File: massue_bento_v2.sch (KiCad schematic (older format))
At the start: 0 parts

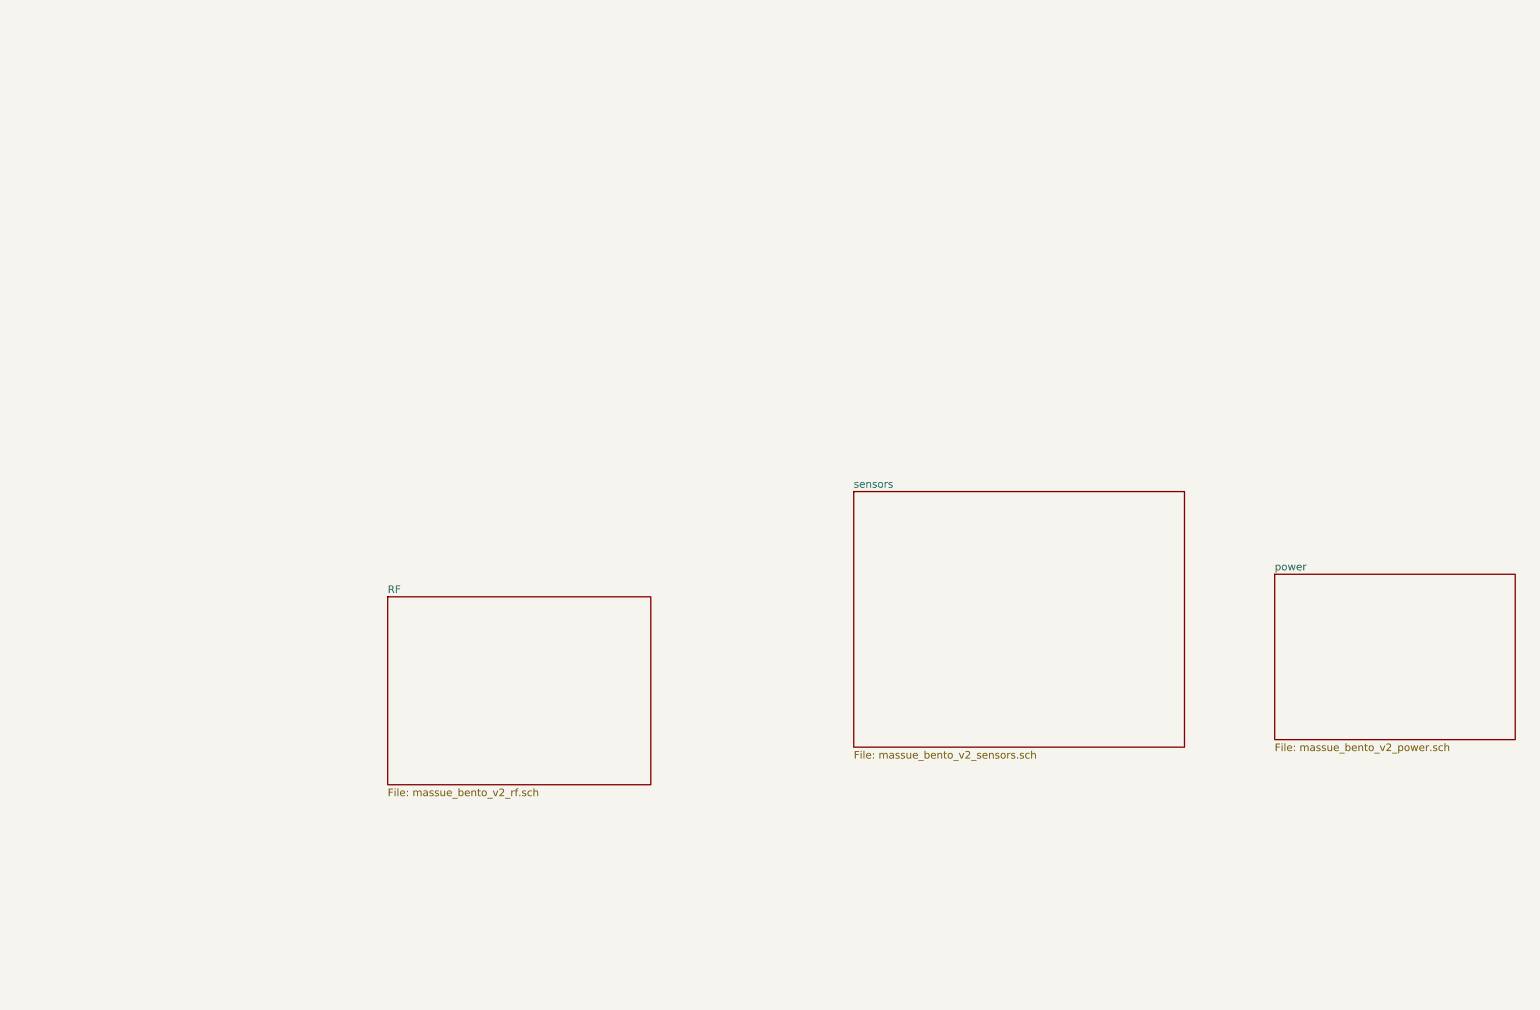
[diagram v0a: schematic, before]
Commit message: New: main MCU connections and Flash memory
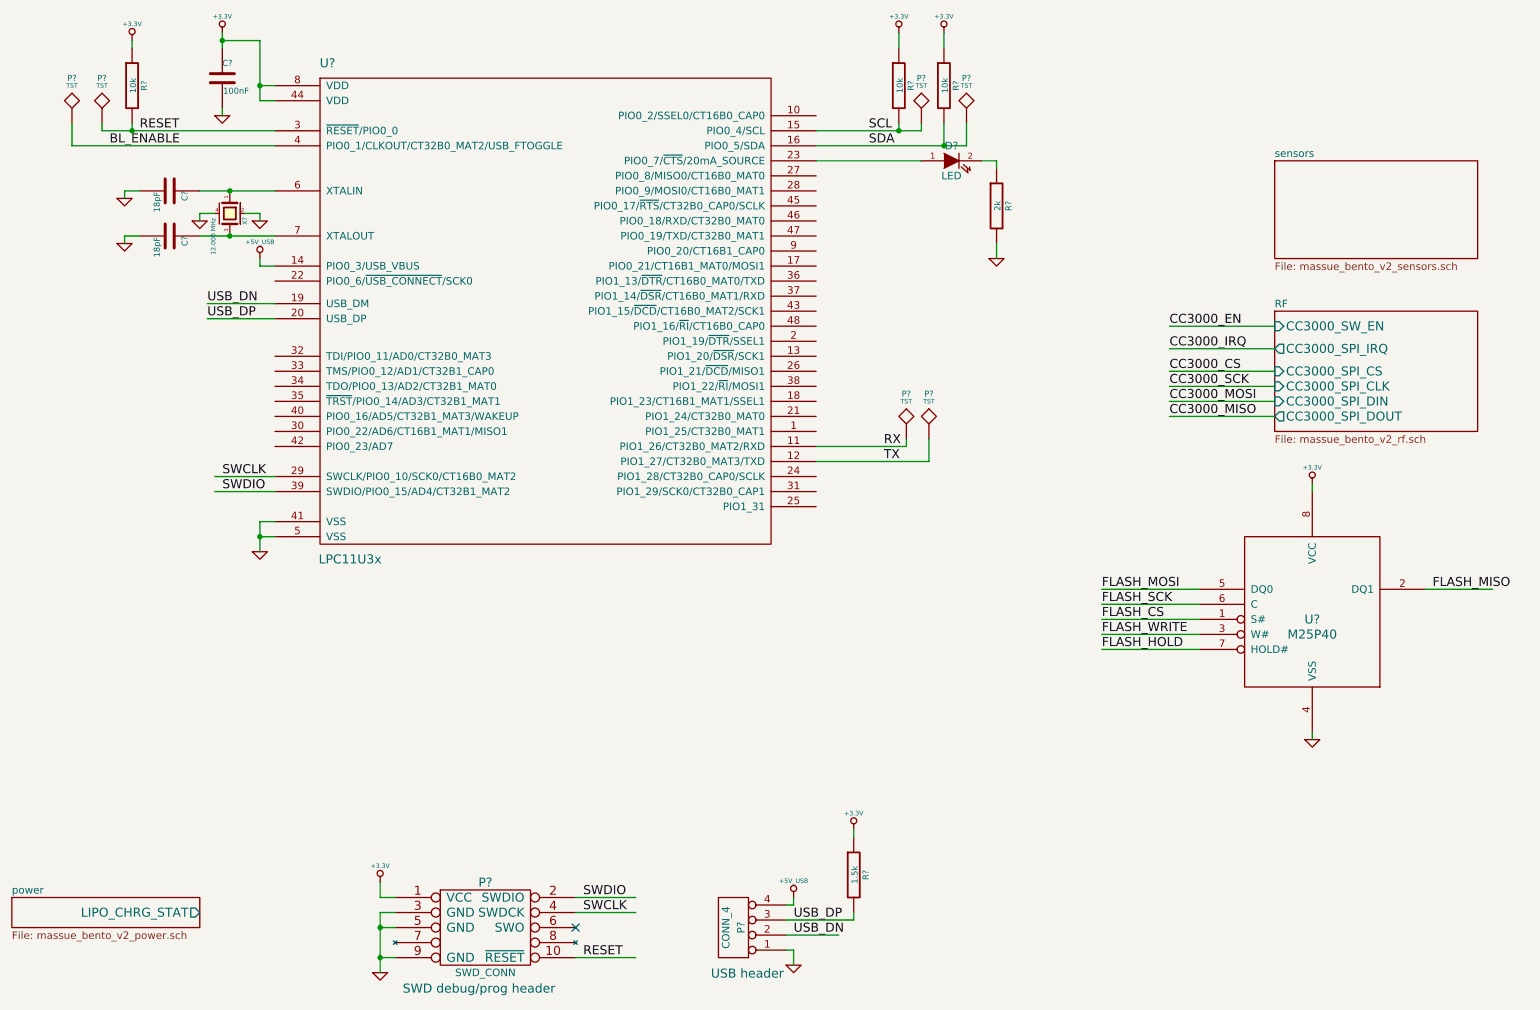
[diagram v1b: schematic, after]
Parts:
- added C?: 100nF, symbol C
- added C? (x2): 18pF, symbol C
- added D?: LED, symbol LED
- added P?: CONN_4, symbol CONN_4
- added P? (x6): TST, symbol TST
- added P?: SWD_CONN, symbol SWD_CONN
- added R? (x3): 10k, symbol R
- added R?: 1.5k, symbol R
- added R?: 2k, symbol R
- added U?: LPC11U3x, symbol LPC11U3x
- added U?: M25P40, symbol M25P40
- added X?: 12.000 MHz, symbol CRYSTAL_SMD_4PIN
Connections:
- net labels added: +3.3V, +5V_USB, BL_ENABLE, CC3000_CS, CC3000_EN, CC3000_IRQ, CC3000_MISO, CC3000_MOSI, CC3000_SCK, FLASH_CS, FLASH_HOLD, FLASH_MISO, FLASH_MOSI, FLASH_SCK, FLASH_WRITE, GND, RESET, RX, SCL, SDA, SWCLK, SWDIO, TX, USB_DN, USB_DP
- wire segments 0 -> 78
- no-connect marks 0 -> 1
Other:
- note added: "SWD debug/prog header"
- note added: "USB header"
